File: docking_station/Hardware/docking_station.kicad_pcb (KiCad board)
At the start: 2 copper layers, 114.5 x 41 mm, 83 parts, among them IC1 VOM1271T, IC2 VOM1271T, IC3 VOM1271T, IC4 VOM1271T, IC5 VOM1271T, J2 XT60, J3 Conn_01x05_Pin, J5 SUPPLY+, J6 SUPPLY-, K1 RELPOL R40N-3021-85-1024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

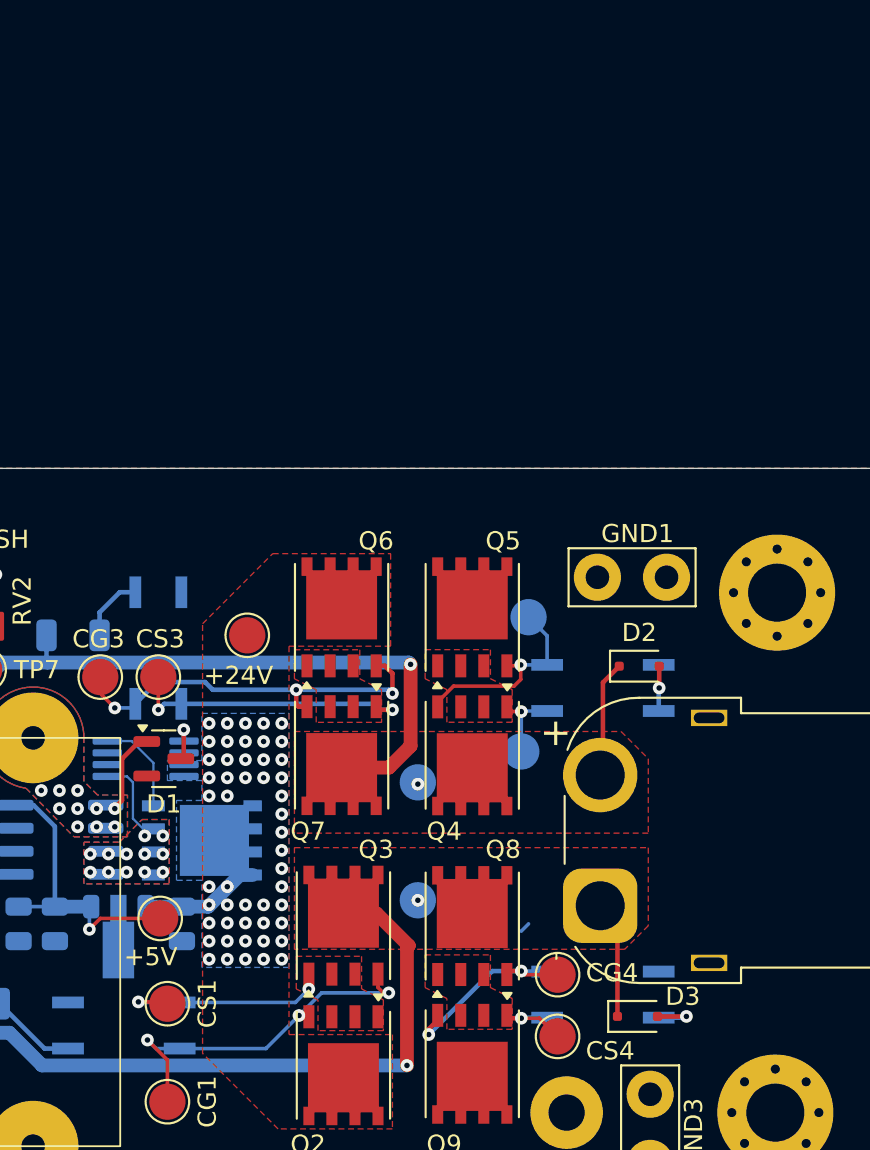
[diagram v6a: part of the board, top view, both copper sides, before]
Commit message: MAJOR: PCB re-do begin
Revert here if needed :P
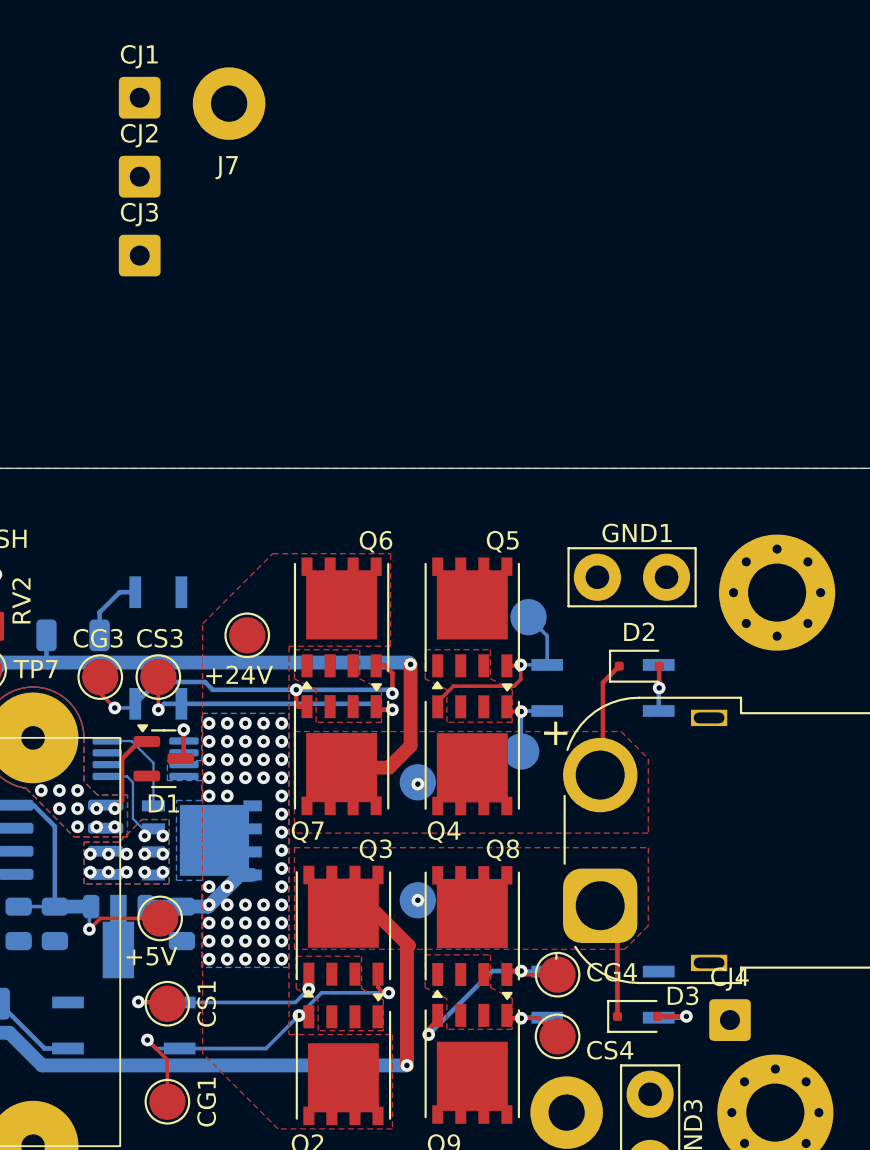
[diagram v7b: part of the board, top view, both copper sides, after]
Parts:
- added CJ1: ~, Connector_Wire:SolderWire-0.5sqmm_1x01_D0.9mm_OD2.3mm, F.Cu at (137.0, 49.1)
- added CJ2: ~, Connector_Wire:SolderWire-0.5sqmm_1x01_D0.9mm_OD2.3mm, F.Cu at (137.0, 53.4)
- added CJ3: ~, Connector_Wire:SolderWire-0.5sqmm_1x01_D0.9mm_OD2.3mm, F.Cu at (137.0, 57.8)
- added CJ4: ~, Connector_Wire:SolderWire-0.5sqmm_1x01_D0.9mm_OD2.3mm, F.Cu at (169.5, 99.9)
- added J7: SUPPLY-, firo_footprints:14 AWG soldering pad, F.Cu at (141.9, 49.4)
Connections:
- IC1 pad 2: Net-(IC1-K_1) -> Net-(CJ1-Pin_1)
- IC2 pad 1: Net-(IC1-K_1) -> Net-(CJ2-Pin_1)
- IC3 pad 2: Net-(IC3-K_1) -> Net-(CJ3-Pin_1)
- IC4 pad 1: Net-(IC3-K_1) -> Net-(CJ4-Pin_1)
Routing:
- net Net-(IC4-A_2): track 13.0 -> 12.4 mm

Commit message: big layout updates
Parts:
- removed H5, H6, H7: MountingHole_Pad, MountingHole:MountingHole_2.2mm_M2_Pad_Via
- removed J7: SUPPLY-, firo_footprints:14 AWG soldering pad
- added J1: WAGO, firo_footprints:WAGO 2601-3102, F.Cu at (97.0, 105.0)
- CJ1, CJ2, CJ3, CJ4: footprint Connector_Wire:SolderWire-0.5sqmm_1x01_D0.9mm_OD2.3mm -> firo_footprints:20AWG SMD; moved to B.Cu
- J5, J6: footprint firo_footprints:14 AWG soldering pad -> firo_footprints:14 AWG THT
- moved CJ2 63.6 mm to (187.8, 91.6), turned to -90 degrees
- moved CJ1 62.1 mm to (149.2, 110.0), turned to -90 degrees
- moved GND2 58.1 mm to (140.9, 121.0), turned to 180 degrees
- moved GND3 43.0 mm to (126.4, 89.0), turned to 180 degrees
- moved CJ3 38.3 mm to (161.3, 87.3), turned to -90 degrees
- moved J6 27.8 mm to (184.1, 119.7)
- moved H3 27.5 mm to (196.0, 90.0)
- moved H2 27.3 mm to (196.0, 118.0)
- moved CG2 27.2 mm to (182.1, 91.0)
- moved CS4 26.9 mm to (183.0, 114.8)
- moved CS2 26.5 mm to (181.0, 98.3)
- moved D3 26.5 mm to (187.4, 112.9)
- moved GND1 26.5 mm to (189.0, 88.7)
- moved IC2 26.5 mm to (185.5, 94.8)
- moved IC4 26.5 mm to (185.5, 111.7)
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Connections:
- net Net-(J5-Pin_1) renamed /SUPPLY+
- C7 pad 1: Net-(U6-+) -> Net-(U6--)
- R10 pad 1: Net-(U6--) -> Net-(U6-+)
- R7 pad 1: Net-(U6-+) -> Net-(U6--)
- R8 pad 1: Net-(U6-+) -> Net-(U6--)
- RV2 pad 2: Net-(U6--) -> Net-(U6-+)
- TP7 pad 1: Net-(U6-+) -> Net-(U6--)
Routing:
- net Net-(J1-Pin_1): track 0.00 -> 51.7 mm
- net Net-(J1-Pin_2): track 0.00 -> 46.6 mm
- net +5V: track 33.0 -> 59.5 mm
- net Net-(CJ4-Pin_1): track 0.00 -> 8.64 mm
- net Net-(CJ1-Pin_1): track 0.00 -> 6.71 mm
- net Net-(IC2-A_2): track 11.5 -> 17.4 mm, vias 1 -> 2
- net Net-(IC4-A_2): track 12.4 -> 17.9 mm
- net Net-(IC5-A_2): track 12.5 -> 15.8 mm
- net /CS_1: track 12.2 -> 15.4 mm
- net Net-(CJ2-Pin_1): track 0.00 -> 2.25 mm
- net Net-(CJ3-Pin_1): track 0.00 -> 2.24 mm
- net Net-(U6-+): track 9.90 -> 7.69 mm, vias 0 -> 1
- net /CS_3: track 15.9 -> 17.5 mm
- net Net-(U6--): track 7.48 -> 8.88 mm, vias 1 -> 0
- net /SUPPLY+: track 4.04 -> 5.29 mm
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- added copper zone on B.Cu, net /SUPPLY+
- added copper zone on F.Cu, net /SUPPLY+
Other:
- board size 114.5 x 41 mm -> 120 x 40 mm
- board text added: "SUPPLY+"
- board text added: "SUPPLY-"
- board text removed: "SUP+"
